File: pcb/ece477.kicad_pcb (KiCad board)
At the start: 2 copper layers, 44 x 40 mm, 23 parts, among them J1 USB_B, SW1 SW_DIP_x01, U1 ESP32-WROOM-32, U2 FT232RL-REEL, U3 LM3671, U4 ADA254, U5 ADA751

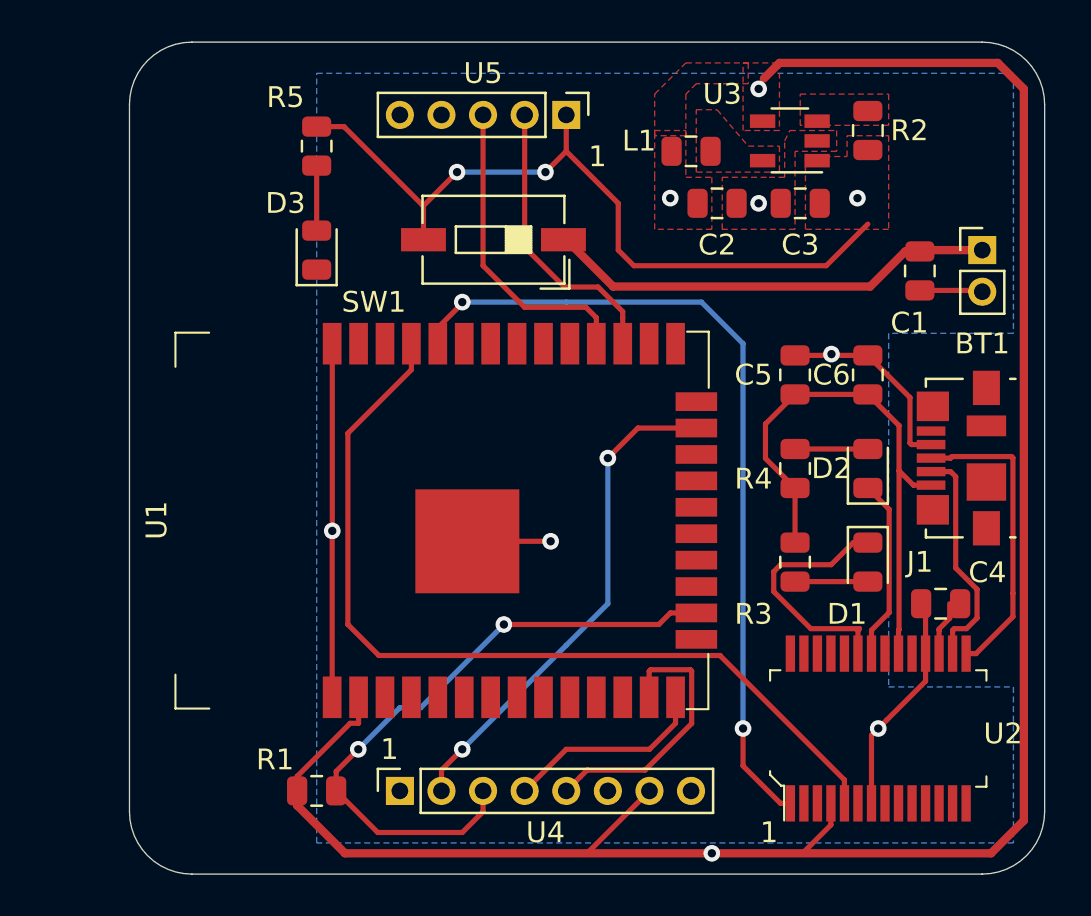
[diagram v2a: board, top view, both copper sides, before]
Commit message: fixed LM3671 ground vias
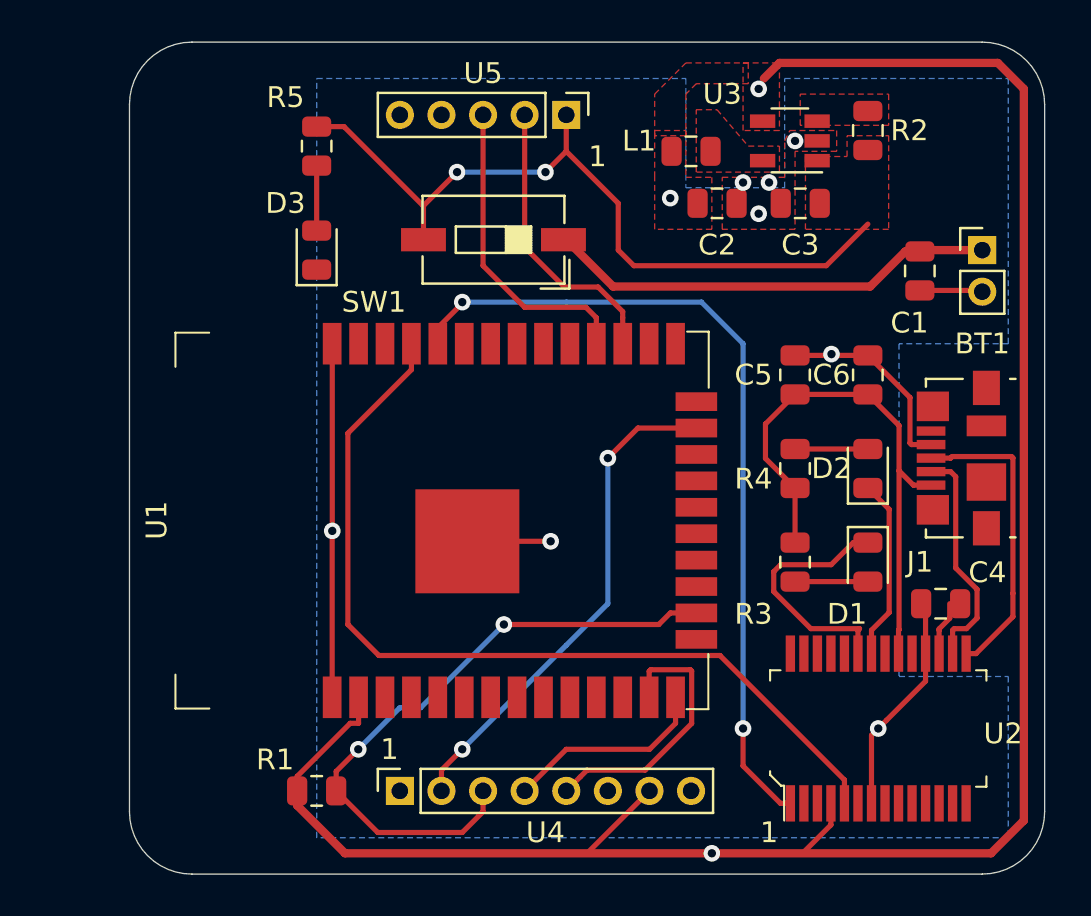
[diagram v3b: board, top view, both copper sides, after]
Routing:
- net Net-(C3-Pad2): vias 3 -> 2
- net GND: vias 5 -> 8
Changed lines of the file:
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@@
     (thickness 1.6)
     (drawings 16)
-    (tracks 195)
+    (tracks 197)
     (zones 0)
     (modules 23)
@@
   (gr_arc (start 144 112) (end 141 112) (angle -90) (layer Edge.Cuts) (width 0.05))
   (gr_arc (start 144 78) (end 144 75) (angle -90) (layer Edge.Cuts) (width 0.05))
-  (via (at 171.25 82.75) (size 0.8) (drill 0.4) (layers F.Cu B.Cu) (net 1))
   (via (at 174.75 90) (size 0.8) (drill 0.4) (layers F.Cu B.Cu) (net 1))
   (segment (start 181.9375 86.9375) (end 182 87) (width 0.25) (layer F.Cu) (net 1))
@@
   (segment (start 179.275 105.725) (end 177.399999 107.600001) (width 0.25) (layer F.Cu) (net 1))
   (segment (start 179.275 104.4) (end 179.275 105.725) (width 0.25) (layer F.Cu) (net 1))
+  (via (at 170.5 81.75) (size 0.8) (drill 0.4) (layers F.Cu B.Cu) (net 1))
+  (via (at 171.75 81.75) (size 0.8) (drill 0.4) (layers F.Cu B.Cu) (net 1))
+  (via (at 171.25 83.25) (size 0.8) (drill 0.4) (layers F.Cu B.Cu) (net 1))
+  (via (at 173 79.75) (size 0.8) (drill 0.4) (layers F.Cu B.Cu) (net 1))
   (segment (start 178.3 85.0625) (end 176.6125 86.75) (width 0.4) (layer F.Cu) (net 2))
   (segment (start 179 85.0625) (end 178.3 85.0625) (width 0.4) (layer F.Cu) (net 2))
@@
   (segment (start 161 81.25) (end 162 80.25) (width 0.25) (layer F.Cu) (net 46))
   (segment (start 162 80.25) (end 162 78.5) (width 0.25) (layer F.Cu) (net 46))
-  (via (at 176 82.5) (size 0.8) (drill 0.4) (layers F.Cu B.Cu) (net 46))
   (segment (start 174.5 85.75) (end 176.5 83.75) (width 0.25) (layer F.Cu) (net 46))
   (segment (start 165.25 85.75) (end 174.5 85.75) (width 0.25) (layer F.Cu) (net 46))
@@
     (polygon
       (pts
-        (xy 183.5 89) (xy 177.5 89) (xy 177.5 106) (xy 183.5 106) (xy 183.5 113.5)
-        (xy 150 113.5) (xy 150 76.5) (xy 183.5 76.5)
+        (xy 167.75 82) (xy 172.5 82) (xy 172.5 76.75) (xy 183.25 76.75) (xy 183.25 89.5)
+        (xy 178 89.5) (xy 178 105.5) (xy 183.25 105.5) (xy 183.25 113.25) (xy 150 113.25)
+        (xy 150 76.75) (xy 167.75 76.75)
       )
     )

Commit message: updated pcb
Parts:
- L1: footprint Inductor_SMD:L_0805_2012Metric -> LQH3NPN2R2MMEL:IND_LQH3NPN2R2MMEL
- moved C4 2.15 mm to (182.0, 101.2)
- moved J1 1.50 mm to (182.5, 95.0)
- moved L1 0.50 mm to (168.0, 79.8)
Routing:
- net GND: track 44.6 -> 80.4 mm, vias 8 -> 9
- net Net-(C4-Pad2): track 2.61 -> 10.5 mm
- net Net-(J1-Pad2): track 11.0 -> 18.0 mm
- net Net-(C5-Pad1): track 26.7 -> 33.5 mm, vias 0 -> 4
- net Net-(J1-Pad3): track 15.3 -> 17.8 mm
- net Net-(BT1-Pad1): vias 0 -> 1
- net Net-(U1-Pad35): vias 0 -> 1
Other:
- board text added: "3.3V"
- board text added: "3.7V"
- board text added: "FB"
- board text added: "RXD"
- board text added: "TXD"

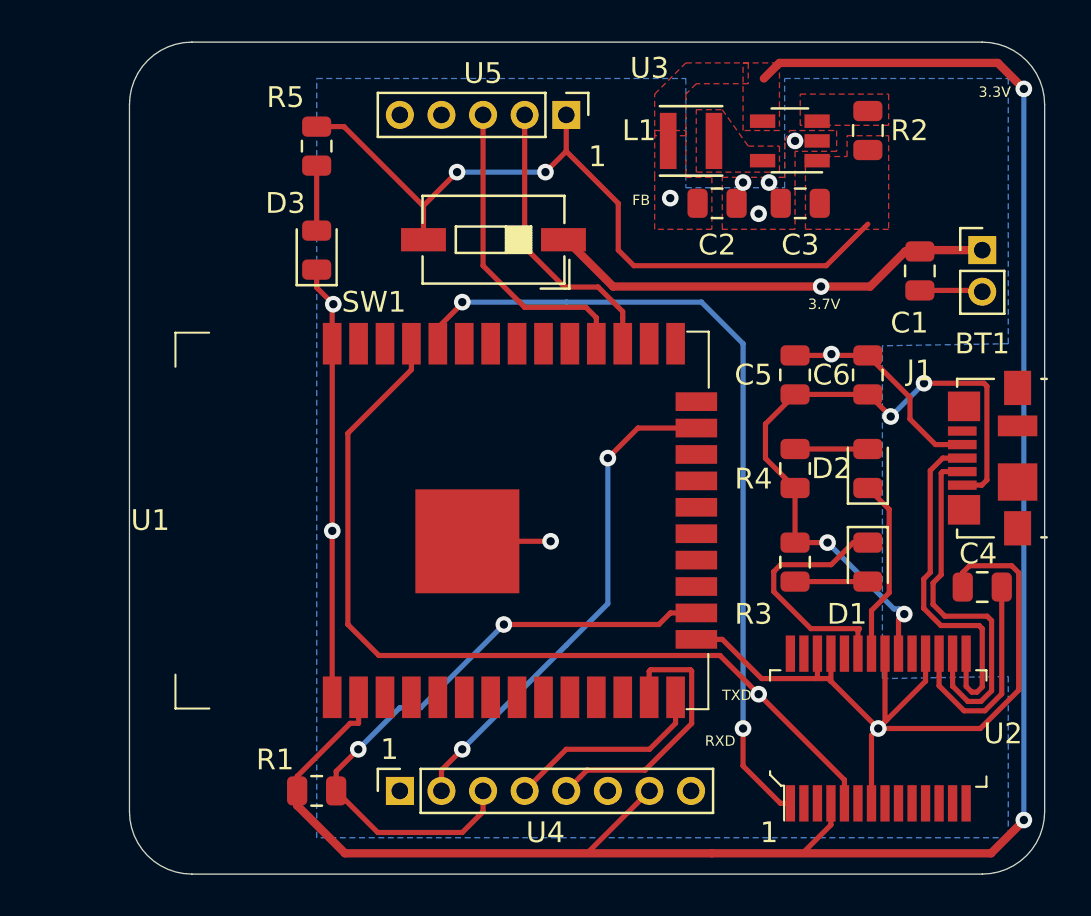
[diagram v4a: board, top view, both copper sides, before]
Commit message: updated pcb pinheader width
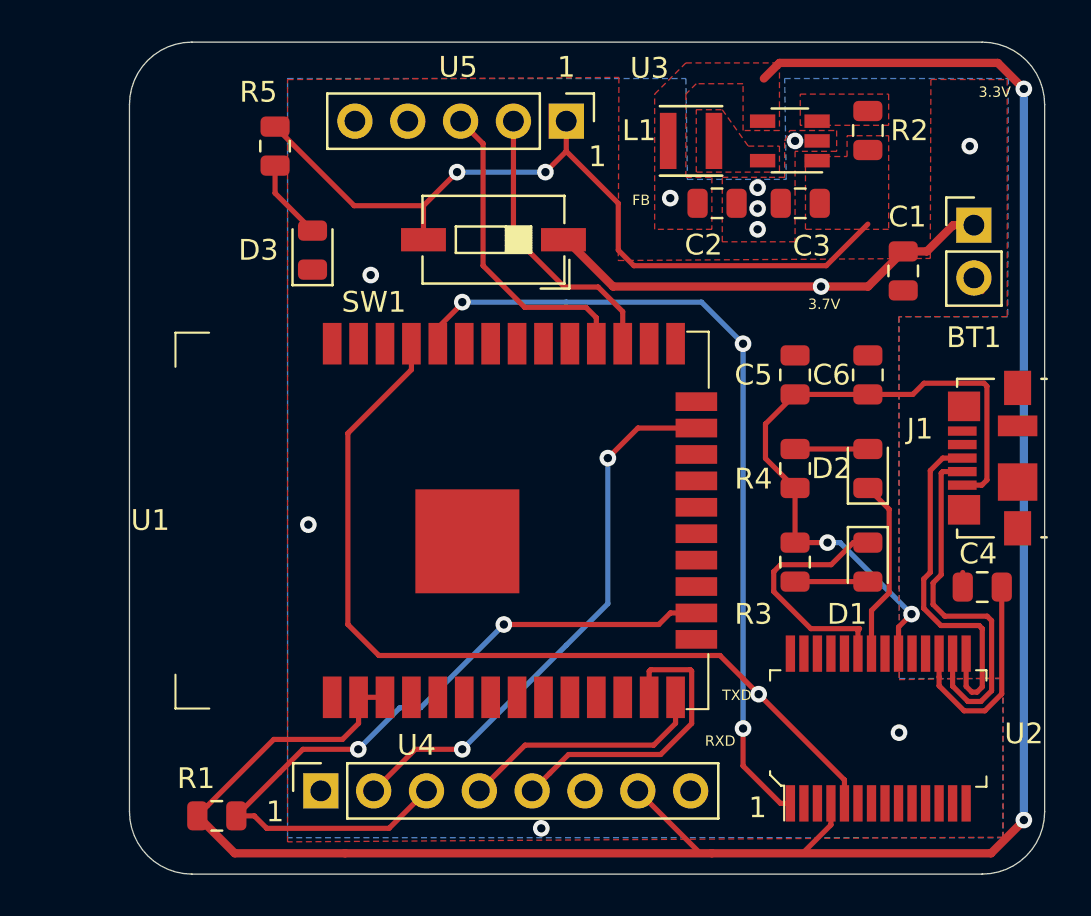
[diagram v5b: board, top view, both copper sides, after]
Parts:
- BT1: footprint Connector_PinHeader_2.00mm:PinHeader_1x02_P2.00mm_Vertical -> Connector_PinHeader_2.54mm:PinHeader_1x02_P2.54mm_Vertical
- U4: footprint Connector_PinSocket_2.00mm:PinSocket_1x08_P2.00mm_Vertical -> Connector_PinSocket_2.54mm:PinSocket_1x08_P2.54mm_Vertical
- U5: footprint Connector_PinHeader_2.00mm:PinHeader_1x05_P2.00mm_Vertical -> Connector_PinHeader_2.54mm:PinHeader_1x05_P2.54mm_Vertical
- moved R1 4.95 mm to (145.2, 112.2)
- moved U4 3.80 mm to (150.2, 111.0)
- moved R5 2.00 mm to (148.0, 80.0)
- moved BT1 1.26 mm to (181.6, 83.8)
- moved C1 0.80 mm to (178.2, 86.0)
- moved U5 0.30 mm to (162.0, 78.8)
- moved D3 0.20 mm to (149.8, 85.0)
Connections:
- U1 pad 25: Net-(U1-Pad25) -> GND
- U1 pad 3: Net-(U1-Pad3) -> Net-(C2-Pad2)
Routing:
- net GND: track 80.4 -> 1.56 mm
- net Net-(C2-Pad2): track 98.9 -> 109.5 mm
- net Net-(R1-Pad2): track 30.7 -> 36.3 mm
- net Net-(U1-Pad23): track 24.2 -> 26.8 mm
- net Net-(U1-Pad14): track 9.85 -> 12.0 mm
- net Net-(C3-Pad2): track 37.0 -> 39.0 mm
- net Net-(U1-Pad13): track 13.2 -> 14.9 mm
- net Net-(D3-Pad2): track 3.12 -> 3.87 mm
- net Net-(C5-Pad1): track 33.5 -> 32.8 mm, vias 4 -> 2
- net Net-(U1-Pad34): vias 2 -> 3

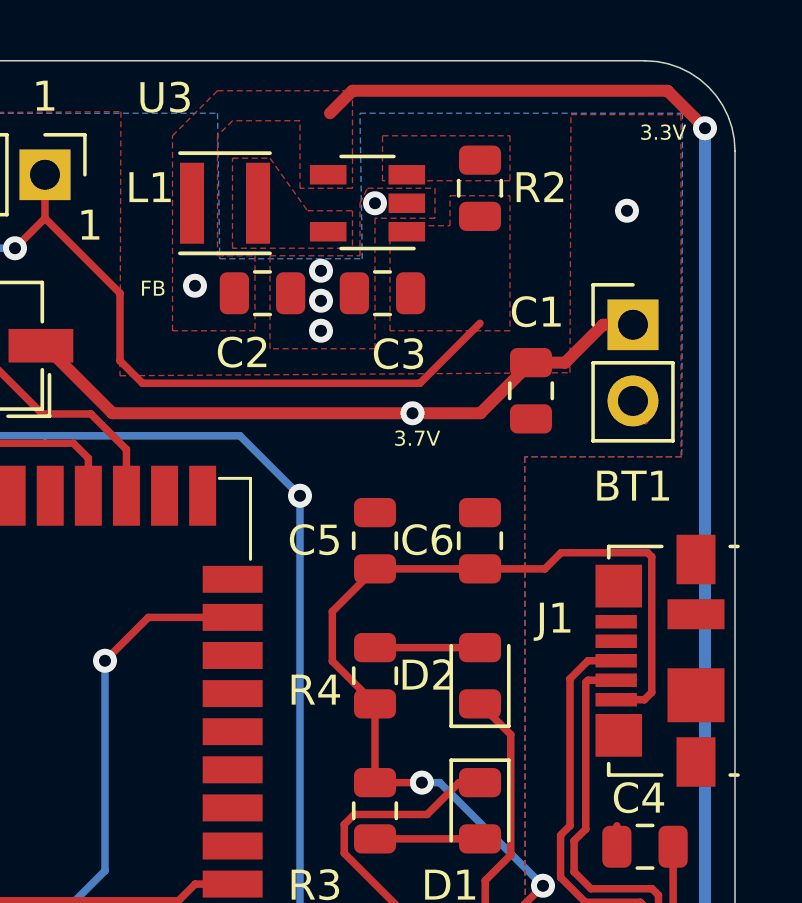
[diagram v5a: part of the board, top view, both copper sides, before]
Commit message: gui-blink added
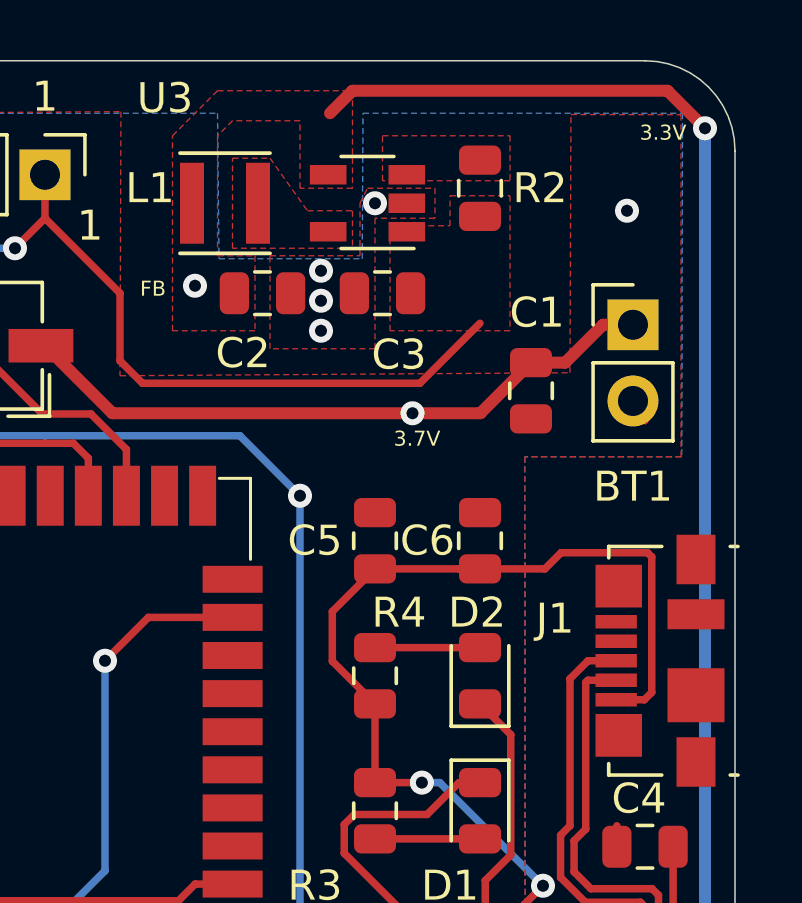
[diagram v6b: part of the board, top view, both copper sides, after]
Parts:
- R2: value 100kΩ -> 10kΩ
- R3, R4: value 1kΩ -> 500Ω
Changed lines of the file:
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@@
       (effects (font (size 1 1) (thickness 0.15)))
     )
-    (fp_text value 1kΩ (at 0 1.65 90) (layer F.Fab)
+    (fp_text value 500Ω (at 0 1.65 90) (layer F.Fab)
       (effects (font (size 1 1) (thickness 0.15)))
     )
@@
     (tags diode)
     (attr smd)
-    (fp_text reference D2 (at 0 -1.75 180) (layer F.SilkS)
+    (fp_text reference D2 (at 2.1 -0.1 180) (layer F.SilkS)
       (effects (font (size 1 1) (thickness 0.15)))
     )
@@
       (effects (font (size 1 1) (thickness 0.15)))
     )
-    (fp_text value 100kΩ (at 0 1.65 90) (layer F.Fab)
+    (fp_text value 10kΩ (at 0 1.65 90) (layer F.Fab)
       (effects (font (size 1 1) (thickness 0.15)))
     )
@@
     (tags resistor)
     (attr smd)
-    (fp_text reference R4 (at -0.5 -2 180) (layer F.SilkS)
-      (effects (font (size 1 1) (thickness 0.15)))
-    )
-    (fp_text value 1kΩ (at 0 1.65 90) (layer F.Fab)
+    (fp_text reference R4 (at 2.1 0.8 180) (layer F.SilkS)
+      (effects (font (size 1 1) (thickness 0.15)))
+    )
+    (fp_text value 500Ω (at 0 1.65 90) (layer F.Fab)
       (effects (font (size 1 1) (thickness 0.15)))
     )
@@
     (polygon
       (pts
-        (xy 167.825 81.6) (xy 172.575 81.6) (xy 172.5 76.75) (xy 183.25 76.75) (xy 183.225 88.2)
+        (xy 167.8 81.6) (xy 172.575 81.6) (xy 172.6 76.75) (xy 183.25 76.75) (xy 183.225 88.2)
         (xy 177.9875 88.2) (xy 178.0125 105.6) (xy 183 105.6) (xy 183 113.25) (xy 148.6 113.25)
         (xy 148.6 76.75) (xy 167.75 76.75)

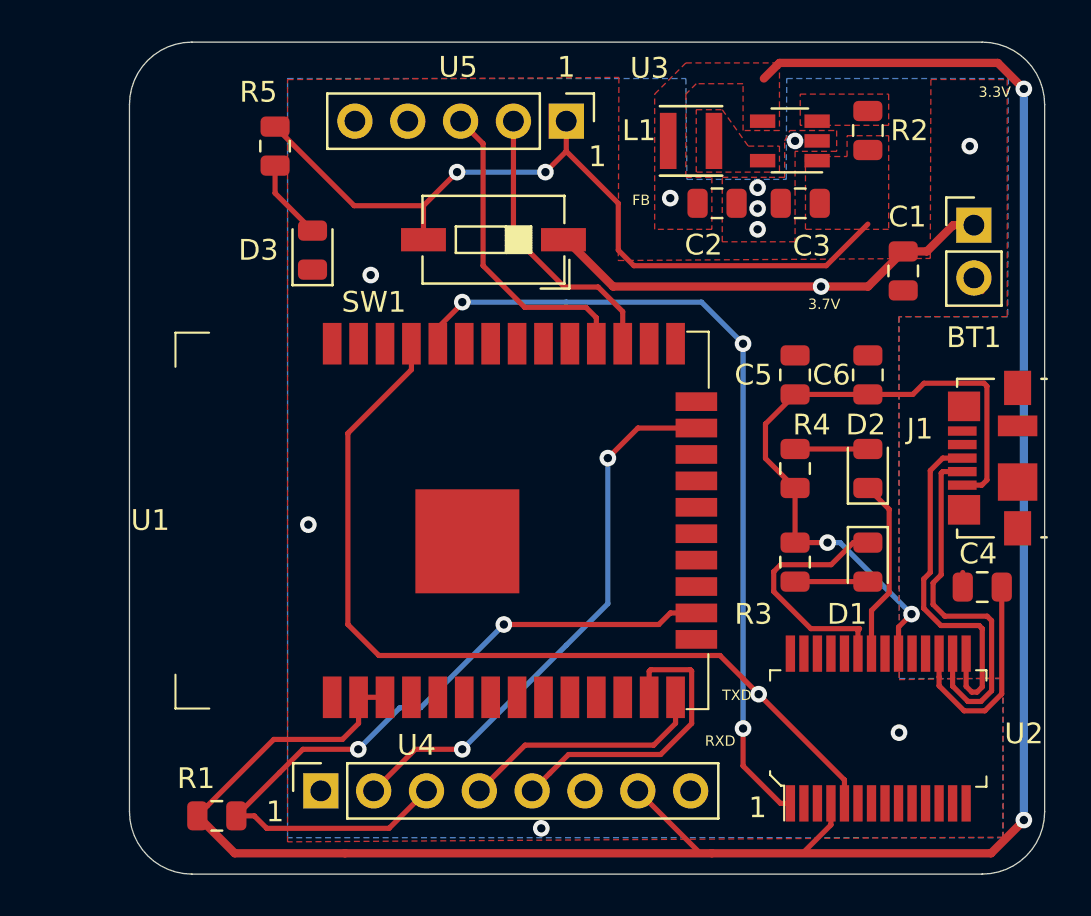
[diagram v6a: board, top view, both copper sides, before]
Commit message: updated pcb with programming transistors
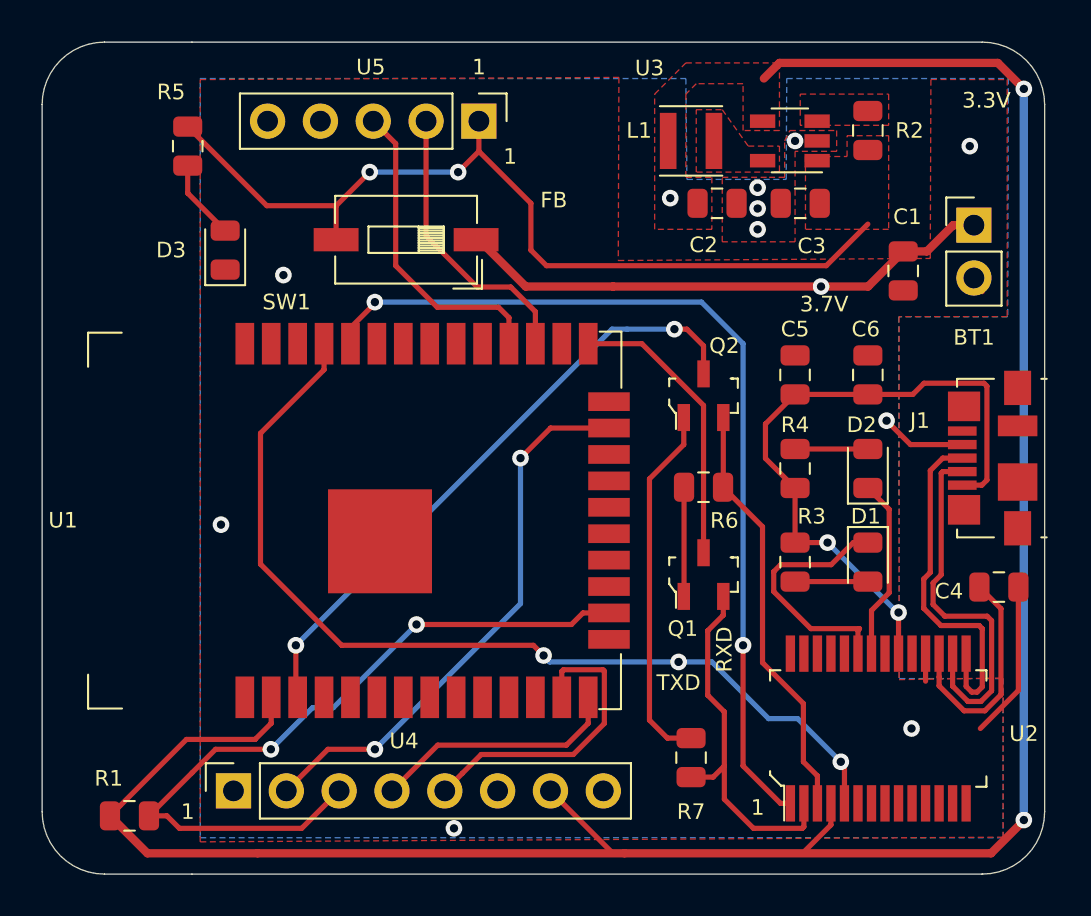
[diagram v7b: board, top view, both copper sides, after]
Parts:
- added Q1: MMBT2222, digikey-footprints:SOT-23-3, F.Cu at (168.6, 100.6)
- added Q2: MMBT2222, digikey-footprints:SOT-23-3, F.Cu at (168.6, 92.0)
- added R6: 1kΩ, Resistor_SMD:R_0805_2012Metric, F.Cu at (168.6, 96.4)
- added R7: 1kΩ, Resistor_SMD:R_0805_2012Metric, F.Cu at (168.0, 109.4)
- moved D3 4.20 mm to (145.6, 85.0)
- moved R1 4.20 mm to (141.0, 112.2)
- moved R5 4.20 mm to (143.8, 80.0)
- moved SW1 4.20 mm to (154.3, 84.5)
- moved U1 4.20 mm to (154.8, 98.0)
- moved U4 4.20 mm to (146.0, 111.0)
- moved U5 4.20 mm to (157.8, 78.8)
- moved C4 0.80 mm to (182.8, 101.2), turned to 180 degrees
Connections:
- U1 pad 25: GND -> Net-(Q1-Pad3)
- U1 pad 3: Net-(C2-Pad2) -> Net-(Q2-Pad3)
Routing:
- net Net-(Q2-Pad3): track 0.00 -> 30.1 mm, vias 0 -> 2
- net Net-(Q2-Pad2): track 0.00 -> 20.4 mm
- net Net-(Q1-Pad2): track 0.00 -> 17.8 mm
- net Net-(Q2-Pad1): track 0.00 -> 17.6 mm
- net Net-(Q1-Pad3): track 0.00 -> 14.6 mm
- net GND: track 1.56 -> 13.1 mm, vias 9 -> 10
- net Net-(Q1-Pad1): track 0.00 -> 5.26 mm
- net Net-(C3-Pad2): track 39.0 -> 43.2 mm
- net Net-(BT1-Pad1): track 21.8 -> 26.0 mm
- net Net-(U1-Pad34): track 40.2 -> 44.4 mm, vias 3 -> 2
- net Net-(C2-Pad2): track 109.5 -> 112.4 mm
- net Net-(U1-Pad35): track 43.6 -> 46.5 mm, vias 1 -> 3
- net Net-(C5-Pad1): track 32.8 -> 32.0 mm
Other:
- board size 44 x 40 mm -> 48.2 x 40 mm
